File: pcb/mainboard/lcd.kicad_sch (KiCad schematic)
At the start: 59 parts, among them J501 0.5mm, J503 0.5mm, U502 TPS65185

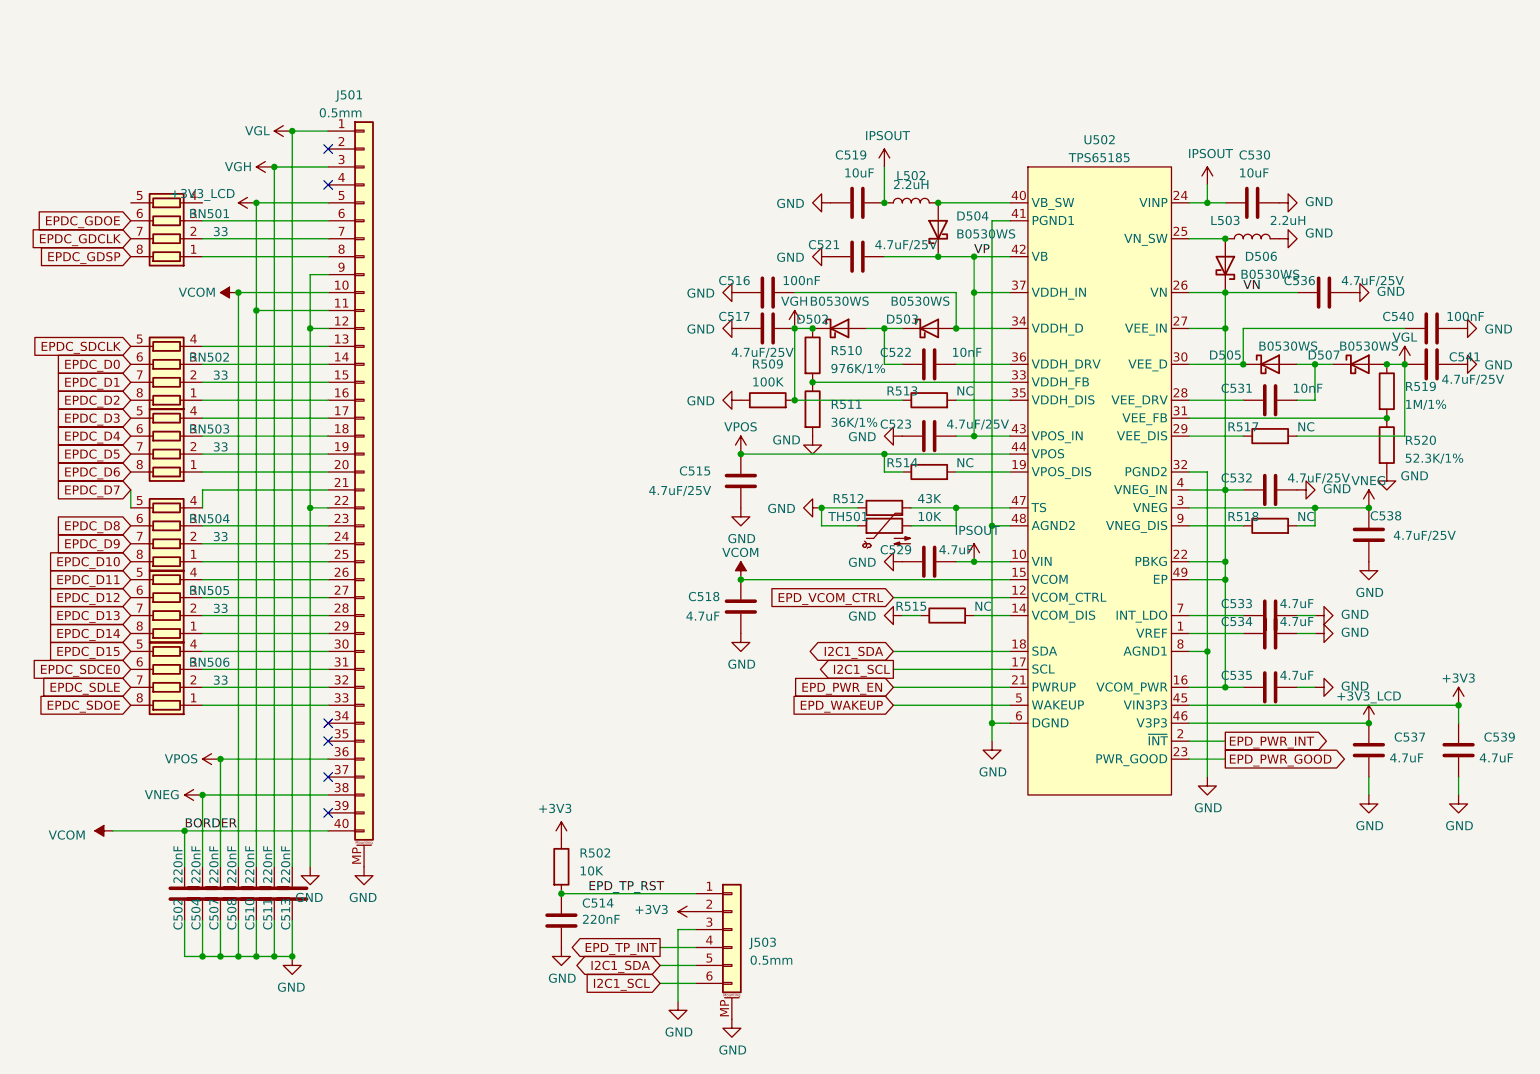
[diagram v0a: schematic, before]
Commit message: pcb: switch to max17135, length tuning for QSPI and SD
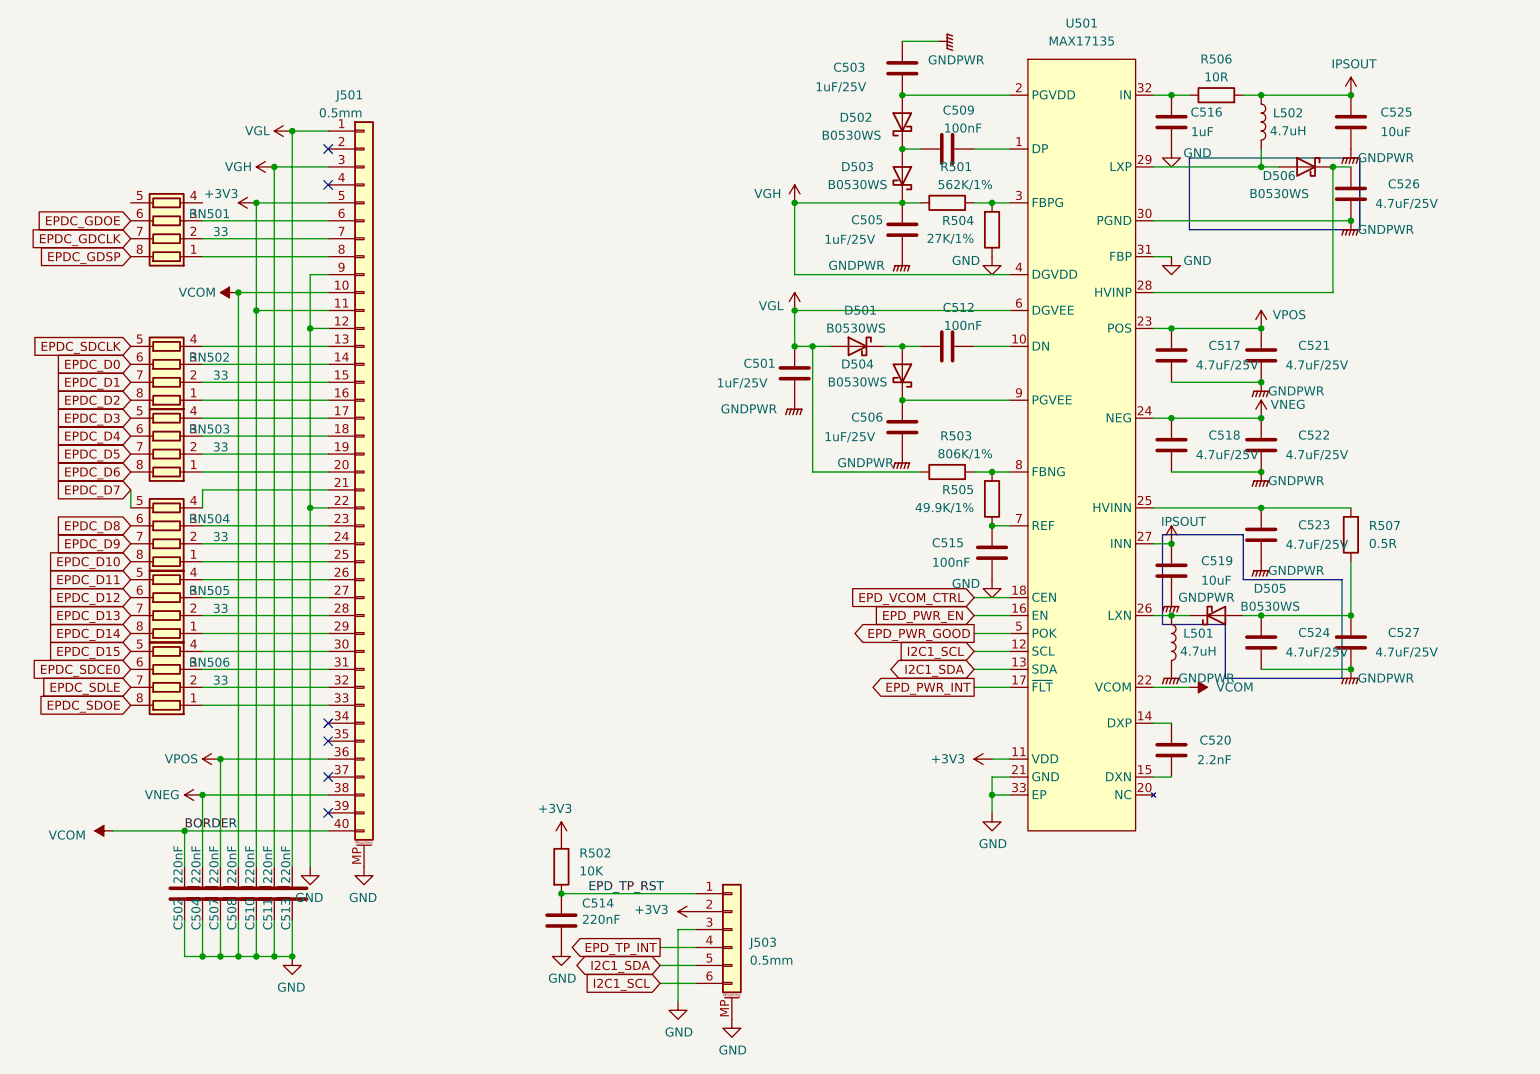
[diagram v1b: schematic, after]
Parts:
- removed C529, C533, C534, C535, C537, C539: 4.7uF, Capacitor_SMD:C_0603_1608Metric, symbol Device:C
- removed C530: 10uF, Capacitor_SMD:C_0603_1608Metric, symbol Device:C
- removed C531: 10nF, Capacitor_SMD:C_0402_1005Metric, symbol Device:C
- removed C532, C536, C538, C541: 4.7uF/25V, Capacitor_SMD:C_0805_2012Metric, symbol Device:C
- removed C540: 100nF, Capacitor_SMD:C_0402_1005Metric, symbol Device:C
- removed D507: B0530WS, Diode_SMD:D_SOD-323, symbol Device:D_Schottky
- removed L503: 2.2uH, footprints:L_1212, symbol Device:L
- removed R509: 100K, Resistor_SMD:R_0402_1005Metric, symbol Device:R
- removed R510: 976K/1%, Resistor_SMD:R_0402_1005Metric, symbol Device:R
- removed R511: 36K/1%, Resistor_SMD:R_0402_1005Metric, symbol Device:R
- removed R512: 43K, Resistor_SMD:R_0402_1005Metric, symbol Device:R
- removed R513, R514, R515, R517, R518: NC, Resistor_SMD:R_0402_1005Metric, symbol Device:R
- removed R519: 1M/1%, Resistor_SMD:R_0402_1005Metric, symbol Device:R
- removed R520: 52.3K/1%, Resistor_SMD:R_0402_1005Metric, symbol Device:R
- removed TH501: 10K, Resistor_SMD:R_0603_1608Metric, symbol Device:Thermistor_NTC
- removed U502: TPS65185, Package_DFN_QFN:QFN-48-1EP_6x6mm_P0.4mm_EP4.2x4.2mm_ThermalVias, symbol symbols:TPS65185
- added C501, C503, C505, C506: 1uF/25V, Capacitor_SMD:C_0805_2012Metric, symbol Device:C
- added C509, C512: 100nF, Capacitor_SMD:C_0402_1005Metric, symbol Device:C
- added C520: 2.2nF, Capacitor_SMD:C_0402_1005Metric, symbol Device:C
- added C524, C526, C527: 4.7uF/25V, Capacitor_SMD:C_0805_2012Metric, symbol Device:C
- added C525: 10uF, Capacitor_SMD:C_0603_1608Metric, symbol Device:C
- added D501: B0530WS, Diode_SMD:D_SOD-323, symbol Device:D_Schottky
- added L501: 4.7uH, footprints:L_1212, symbol Device:L
- added R501: 562K/1%, Resistor_SMD:R_0402_1005Metric, symbol Device:R
- added R503: 806K/1%, Resistor_SMD:R_0402_1005Metric, symbol Device:R
- added R504: 27K/1%, Resistor_SMD:R_0402_1005Metric, symbol Device:R
- added R505: 49.9K/1%, Resistor_SMD:R_0402_1005Metric, symbol Device:R
- added R506: 10R, Resistor_SMD:R_0402_1005Metric, symbol Device:R
- added R507: 0.5R, Resistor_SMD:R_0603_1608Metric, symbol Device:R
- added U501: MAX17135, Package_DFN_QFN:QFN-32-1EP_5x5mm_P0.5mm_EP3.1x3.1mm_ThermalVias, symbol symbols:MAX17135
- C515: value 4.7uF/25V -> 100nF; footprint Capacitor_SMD:C_0805_2012Metric -> Capacitor_SMD:C_0402_1005Metric
- C516: value 100nF -> 1uF
- C518: value 4.7uF -> 4.7uF/25V; footprint Capacitor_SMD:C_0603_1608Metric -> Capacitor_SMD:C_0805_2012Metric
- C522: value 10nF -> 4.7uF/25V; footprint Capacitor_SMD:C_0402_1005Metric -> Capacitor_SMD:C_0805_2012Metric
- L502: value 2.2uH -> 4.7uH
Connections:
- net +3V3_LCD is gone; now on net +3V3: C510.1, J501.11 (Pin_11), J501.5 (Pin_5)
- net +3V3: now also U501.11 (VDD)
- net EPD_PWR_EN: now also U501.16 (EN)
- net EPD_PWR_GOOD: now also U501.5 (POK)
- net EPD_PWR_INT: now also U501.17 (~{FLT})
- net EPD_VCOM_CTRL: now also U501.18 (CEN)
- net GND: now also R504.1, U501.21 (GND), U501.31 (FBP), U501.33 (EP); no longer C517.1, C518.1, C519.1, C521.1, C523.1
- net I2C1_SCL: now also U501.12 (SCL)
- net I2C1_SDA: now also U501.13 (SDA)
- net IPSOUT: now also C525.2, R506.2, U501.27 (INN)
- net VCOM: now also U501.22 (VCOM); no longer C518.2
- net VGH: now also D503.1 (K), C505.2, R501.1, U501.4 (DGVDD); no longer C517.2, D502.1 (K)
- net VGL: now also C501.2, D501.2 (A), R503.1, U501.6 (DGVEE)
- net VNEG: now also C518.2, C522.2, U501.24 (NEG)
- net VPOS: now also C517.2, C521.2, U501.23 (POS); no longer C515.2
- net at D505.1 (K): now also L501.1, U501.26 (LXN)
- net at D504.2 (A): now also C512.1, D501.1 (K); no longer L502.2
- net at D505.2 (A): now also C524.2, C527.2, R507.1
- net at C516.2: now also R506.1, U501.32 (IN); no longer D503.2 (A)
- net at D506.2 (A): now also L502.2, U501.29 (LXP)
- net VN: no longer names the net of D506.1 (K)
- net VN: now also C526.2, U501.28 (HVINP)
- removed net VP: C521.2, C523.2, D504.1 (K)
- new net: C523.2, R507.2, U501.25 (HVINN)
- new net: C512.2, U501.10 (DN)
- new net: C506.2, D504.1 (K), U501.9 (PGVEE)
- new net: C520.1, U501.15 (DXN)
- new net: C520.2, U501.14 (DXP)
- new net: C515.2, R505.1, U501.7 (REF)
- new net: R503.2, R505.2, U501.8 (FBNG)
- new net: C509.2, U501.1 (DP)
- new net: U501.19 (NC), U501.20 (NC)
- new net: C503.1, D502.2 (A), U501.2 (PGVDD)
- new net: R501.2, R504.2, U501.3 (FBPG)
- new net: C509.1, D502.1 (K), D503.2 (A)
- new net GNDPWR: C501.1, C503.2, C505.1, C506.1, C517.1, C518.1, C519.1, C521.1, C522.1, C523.1, C524.1, C525.1, C526.1, C527.1, L501.2, U501.30 (PGND)
